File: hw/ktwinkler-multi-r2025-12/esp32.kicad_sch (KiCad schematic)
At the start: 14 parts, among them U3 ESP32-C3FH4, Y2 Q13FC13500004, Y3 XL2EL89CPI-111YLC-40M

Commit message: ktwinkler hw dev: progress stash
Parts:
- removed R3: 0R, Resistor_SMD:R_0603_1608Metric, symbol karl-atomic-basic:KR0603_0R
- added J5: Conn_01x03, Connector_PinHeader_2.54mm:PinHeader_1x03_P2.54mm_Vertical, symbol Connector_Generic:Conn_01x03
- added R3: 0R, Resistor_SMD:R_0402_1005Metric, symbol karl-atomic-basic:KR0402_0R
- added R9: 470R, Resistor_SMD:R_0402_1005Metric, symbol karl-atomic-basic:KR0402_470R
- added SW1: BOOT, Button_Switch_SMD:SW_SPST_TL3342, symbol Switch:SW_Push
- AE1: value Antenna_Dipole -> Antenna_lolpole
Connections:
- net +3V3: now also C13.1, C14.1, C2.1
- net GND: now also C13.2, C14.2, C2.2, J5.1 (Pin_1)
- net at AE1.1: now also R3.2
- net at U3.1 (LNA_IN): now also R3.1
- net at U3.27 (U0RXD): now also J5.2 (Pin_2)
- net at U3.28 (U0TXD): now also R9.2
- new net: J5.3 (Pin_3), R9.1
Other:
- note added: "double check vddspi on fh4 package"
- moved on the sheet: AE1, C13, C14, C2

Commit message: pushing onwards like a madlad
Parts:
- added C17, C7, C8: 1uF, Capacitor_SMD:C_0603_1608Metric, symbol karl-atomic-basic:KC0603_1uF
- added C18: 2.2pF, Capacitor_SMD:C_0402_1005Metric, symbol karl-atomic-basic:KC0402_2.2pF
- added J9: BWU.FL-IPEX1, Connector_Coaxial:U.FL_Hirose_U.FL-R-SMT-1_Vertical, symbol karl-parts:BWU.FL-IPEX1
- added L2: 1nH, Inductor_SMD:L_0402_1005Metric, symbol Device:L_Small
- added R10, R11, R12, R13: 10k, Resistor_SMD:R_0402_1005Metric, symbol karl-atomic-basic:KR0402_10k
- added R15, R16: 0R, Resistor_SMD:R_0402_1005Metric, symbol karl-atomic-basic:KR0402_0R
- added SW2: BOOT, Button_Switch_SMD:SW_SPST_TL3342, symbol Switch:SW_Push
- SW1: value BOOT -> RESET
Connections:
- net +3V3: now also U3.18 (VDD_SPI), C17.1, C7.1, C8.1, R10.1, R11.2, R12.1, R13.1
- net GND: now also AE1.2, SW1.2, C17.2, C18.2, C7.2, C8.2, J9.2 (Ext), L2.1, SW2.1
- net at SW1.1: now also U3.7 (CHIP_EN), R11.1
- net at U3.1 (LNA_IN): now also L2.2, R16.1; no longer R3.1
- net PWM8: now reaches U3.10 (MTDI)
- net at U3.14 (GPIO8): now also R12.2
- net at U3.15 (GPIO9): now also R13.2, SW2.2
- net PWM7: now reaches U3.16 (GPIO10)
- net PWM1: now reaches U3.19 (SPIHD)
- net PWM2: now reaches U3.20 (SPIWP)
- net PWM3: now reaches U3.21 (SPICS0)
- net PWM4: now reaches U3.22 (SPICLK)
- net PWM5: now reaches U3.23 (SPID)
- net PWM6: now reaches U3.24 (SPIQ)
- net at U3.6 (GPIO2): now also R10.2
- net MODE: now reaches U3.8 (GPIO3)
- new net: C18.1, R15.2, R16.2, R3.1
- new net: J9.1 (In), R15.1
- no-connect marks 1 -> 0
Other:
- note added: "1pair each for vdd_cpu, vdda, and vdd3p3"
- note added: "MODE is on GPIO3 as that's RTC power zone available, in case we need that for wakeups or something"
- note removed: "double check vddspi on fh4 package"
- moved on the sheet: AE1, C10, C11, C12, C13, C14, C2, C9, J5, R3, R4, R5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

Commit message: ready for scope creep
I think the schematic is ... mostly ok?  I need to decide how much of
the han p1 port scope creep to bother doing, or not...

I've roughyl blocked out the board, seems as good as any?
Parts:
- removed R11, R13: 10k, Resistor_SMD:R_0402_1005Metric, symbol karl-atomic-basic:KR0402_10k
- removed R4, R5: 0R, Resistor_SMD:R_0402_1005Metric, symbol karl-atomic-basic:KR0402_22R
- removed SW1: RESET, Button_Switch_SMD:SW_SPST_TL3342, symbol Switch:SW_Push
- removed SW2: BOOT, Button_Switch_SMD:SW_SPST_TL3342, symbol Switch:SW_Push
- removed Y3: XL2EL89CPI-111YLC-40M, Crystal:Crystal_SMD_3225-4Pin_3.2x2.5mm, symbol karl-parts:XL2EL89CPI-111YLC-40M
- added Y1: 40M, Crystal:Crystal_SMD_2016-4Pin_2.0x1.6mm, symbol karl-parts:Crystal_40M_2016_TAXM40M4ZHBCDT2T
- AE1: footprint (none) -> RF_Experiments:ANT-YOLOPOLE
- Y2: value Q13FC13500004 -> 32k
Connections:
- net GND: now also Y1.2, Y1.4
- net USBDM: now also U3.25 (GPIO18)
- net USBDP: now also U3.26 (GPIO19)
- net RESET_ESP: now reaches U3.7 (CHIP_EN)
- net GBOOT: now reaches U3.15 (GPIO9)
- net at C11.2, U3.29 (XTAL_N): now also Y1.3
- net at C12.1, U3.30 (XTAL_P): now also Y1.1

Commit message: this is just getting silly
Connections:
- net P1IN: now reaches U3.13 (MTDO)
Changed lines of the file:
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@@
+	(wire
+		(pts
+			(xy 154.94 111.76) (xy 167.64 111.76)
+		)
+		(stroke
+			(width 0)
+			(type default)
+		)
+	)
 	(wire
 		(pts
@@
 		)
 	)
+	(hierarchical_label "P1IN"
+		(shape input)
+		(at 167.64 111.76 0)
+		(effects
+			(font
+				(size 1.27 1.27)
+			)
+			(justify left)
+		)
+	)

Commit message: "schematic complete" (lol)
but yeah, i think this is most of it?  time to maybe route shit?
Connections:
- net P1_Req_Out: now reaches U3.12 (MTCK)
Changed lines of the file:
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@@
+	(wire
+		(pts
+			(xy 154.94 109.22) (xy 167.64 109.22)
+		)
+		(stroke
+			(width 0)
+			(type default)
+		)
+	)
 	(wire
 		(pts
@@
 		)
 	)
+	(hierarchical_label "P1_Req_Out"
+		(shape output)
+		(at 167.64 109.22 0)
+		(effects
+			(font
+				(size 1.27 1.27)
+			)
+			(justify left)
+		)
+	)

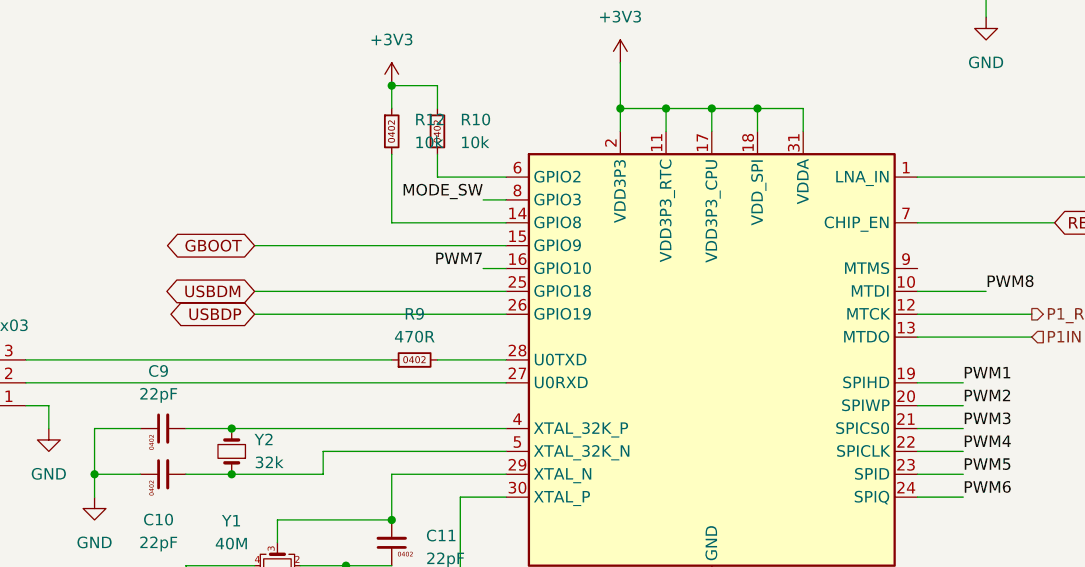
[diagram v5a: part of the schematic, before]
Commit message: update following ERC and symbol fixes
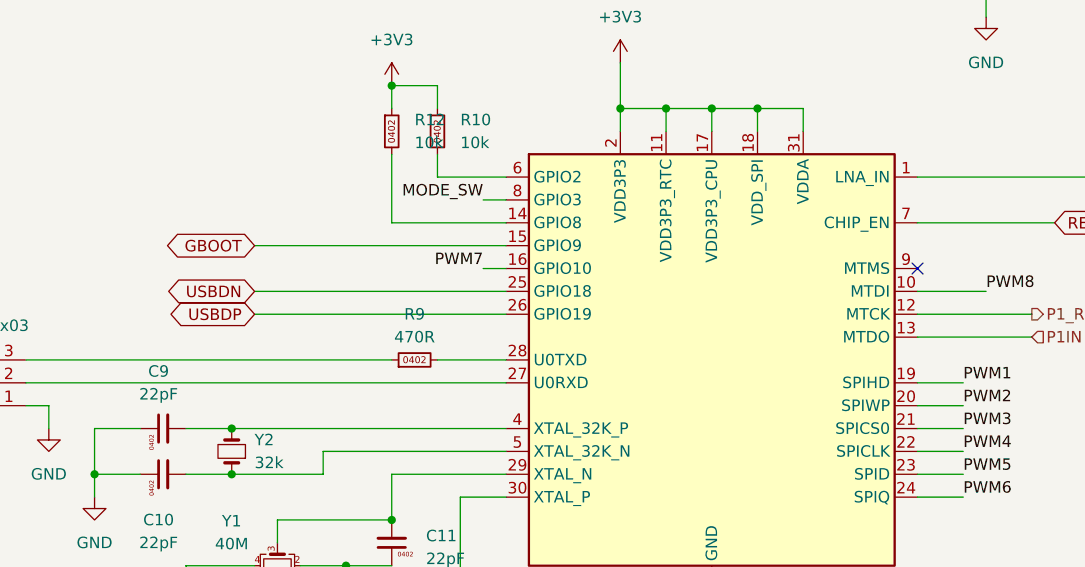
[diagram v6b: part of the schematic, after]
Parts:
- J9: symbol karl-parts:BWU.FL-IPEX1 -> karl-parts:Connector_BWU.FL-IPEX1
- Y2: symbol karl-atomic-basic:Q13FC13500004 -> karl-atomic-basic:Crystal_32k_3215_Q13FC13500004
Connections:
- net USBDM renamed USBDN
- no-connect marks 0 -> 1
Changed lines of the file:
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@@
 		(color 0 0 0 0)
 	)
+	(no_connect
+		(at 154.94 104.14)
+	)
 	(wire
 		(pts
@@
 		)
 	)
-	(global_label "USBDM"
+	(global_label "USBDN"
 		(shape bidirectional)
 		(at 81.28 106.68 180)
@@
 		)
 		(property "Intersheetrefs" "${INTERSHEET_REFS}"
-			(at 70.6521 106.68 0)
+			(at 70.773 106.68 0)
 			(effects
 				(font
@@
 	)
 	(symbol
-		(lib_id "karl-atomic-basic:Q13FC13500004")
+		(lib_id "karl-atomic-basic:Crystal_32k_3215_Q13FC13500004")
 		(at 78.74 124.46 90)
 		(unit 1)
@@
 	)
 	(symbol
-		(lib_id "karl-parts:BWU.FL-IPEX1")
+		(lib_id "karl-parts:Connector_BWU.FL-IPEX1")
 		(at 238.76 106.68 270)
 		(unit 1)

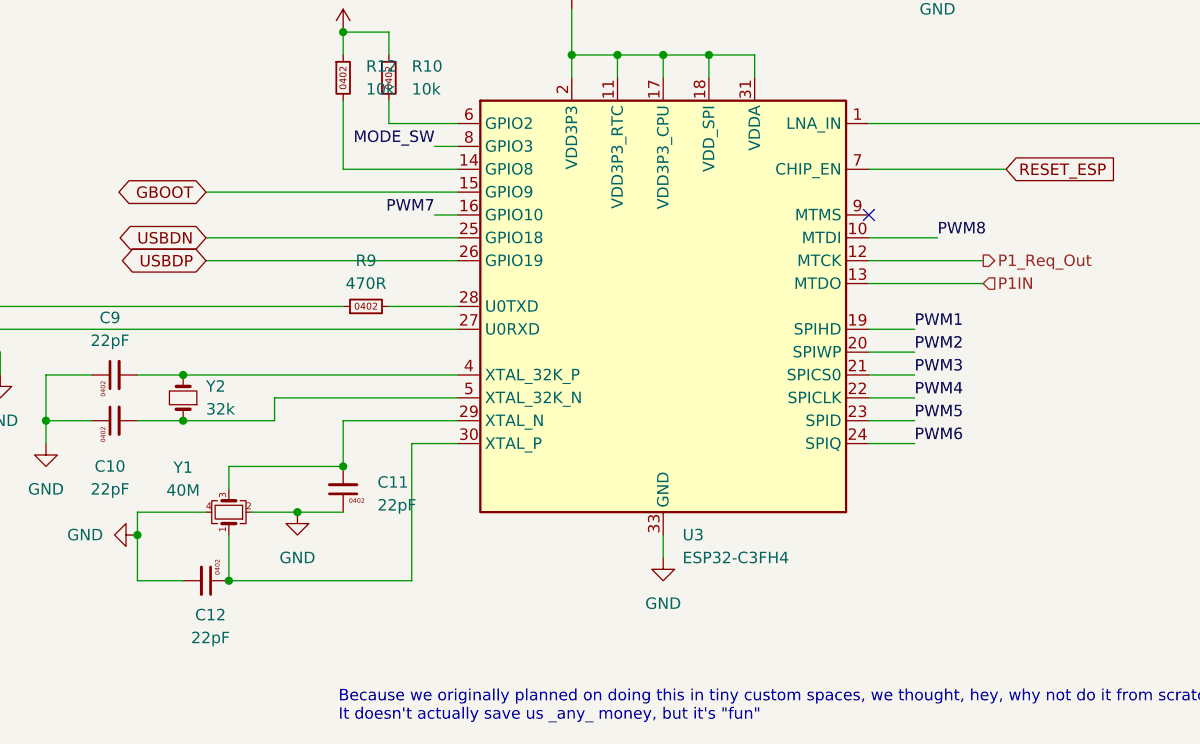
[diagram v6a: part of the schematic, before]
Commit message: streammmm updates
"complete" apart from finishing those antennas.
needs DRC cleanups on both the wch inv-f and also the yolo-pole.
need to at least _basically_ get the antenna trace basic wdith correct
as well.  yolo is fine, when it's guided yolo, not "lol"
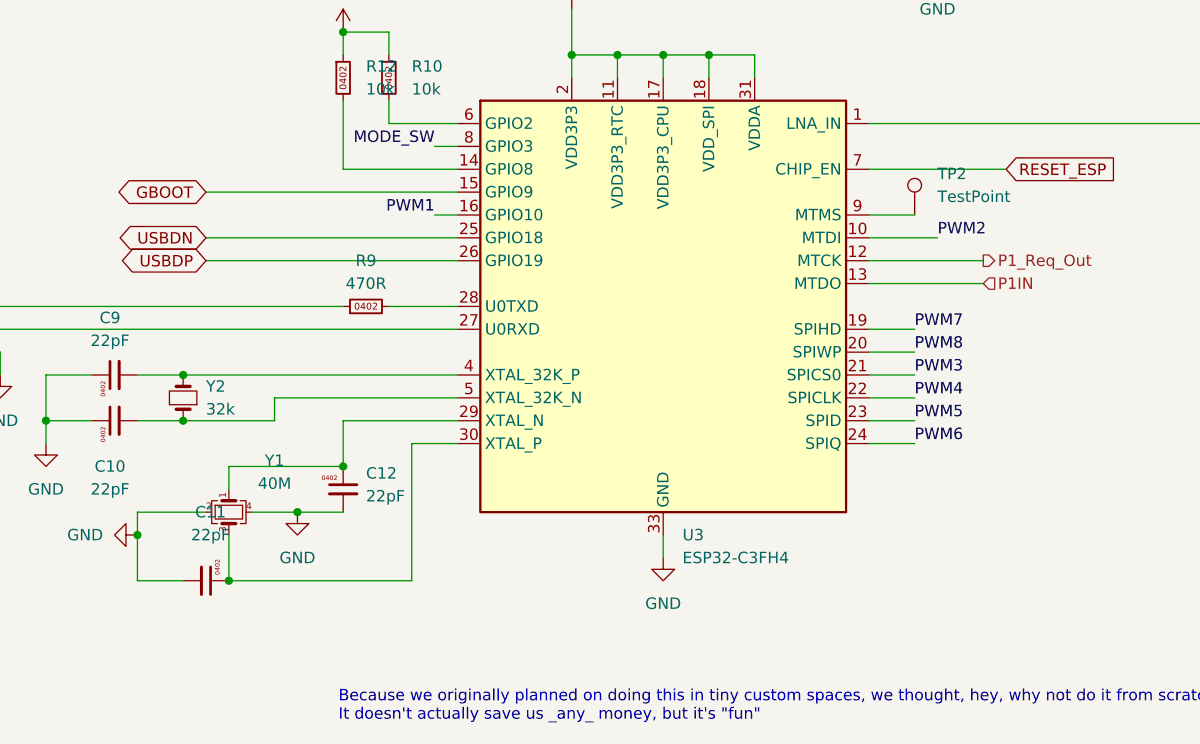
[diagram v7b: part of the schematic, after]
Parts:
- added TP2: TestPoint, TestPoint:TestPoint_THTPad_D1.0mm_Drill0.5mm, symbol Connector:TestPoint
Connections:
- net GND: now also C11.2; no longer C11.1
- net PWM1: now also U3.16 (GPIO10); no longer U3.19 (SPIHD)
- net PWM2: now also U3.10 (MTDI); no longer U3.20 (SPIWP)
- net PWM7: now also U3.19 (SPIHD); no longer U3.16 (GPIO10)
- net PWM8: now also U3.20 (SPIWP); no longer U3.10 (MTDI)
- net at C12.1, Y1.1: now also U3.29 (XTAL_N); no longer U3.30 (XTAL_P)
- net at U3.9 (MTMS): now also TP2.1
- new net: C11.1, U3.30 (XTAL_P), Y1.3
- no-connect marks 1 -> 0
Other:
- moved on the sheet: C11, C12, Y1
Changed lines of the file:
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@@
 	)
 	(junction
-		(at 96.52 132.08)
-		(diameter 0)
-		(color 0 0 0 0)
-	)
-	(junction
 		(at 238.76 93.98)
 		(diameter 0)
@@
 	)
 	(junction
+		(at 220.98 93.98)
+		(diameter 0)
+		(color 0 0 0 0)
+	)
+	(junction
 		(at 83.82 144.78)
 		(diameter 0)
@@
 	)
 	(junction
-		(at 220.98 93.98)
+		(at 96.52 132.08)
 		(diameter 0)
 		(color 0 0 0 0)
@@
 		(color 0 0 0 0)
 	)
-	(no_connect
-		(at 154.94 104.14)
-	)
 	(wire
 		(pts
@@
 	(wire
 		(pts
+			(xy 154.94 104.14) (xy 160.02 104.14)
+		)
+		(stroke
+			(width 0)
+			(type default)
+		)
+	)
+	(wire
+		(pts
 			(xy 127 86.36) (xy 132.08 86.36)
 		)
@@
 	)
 	(label "PWM1"
-		(at 160.02 116.84 0)
+		(at 106.68 104.14 180)
 		(effects
 			(font
 				(size 1.27 1.27)
 			)
-			(justify left bottom)
+			(justify right bottom)
 		)
 	)
 	(label "PWM8"
-		(at 162.56 106.68 0)
+		(at 160.02 119.38 0)
 		(effects
 			(font
@@
 	)
 	(label "PWM2"
-		(at 160.02 119.38 0)
+		(at 162.56 106.68 0)
 		(effects
 			(font
@@
 	)
 	(label "PWM7"
-		(at 106.68 104.14 180)
+		(at 160.02 116.84 0)
 		(effects
 			(font
 				(size 1.27 1.27)
 			)
-			(justify right bottom)
+			(justify left bottom)
 		)
 	)
@@
 	(symbol
 		(lib_id "karl-parts:Crystal_40M_2016_TAXM40M4ZHBCDT2T")
-		(at 83.82 137.16 90)
+		(at 83.82 137.16 270)
 		(unit 1)
 		(exclude_from_sim no)
@@
 		(fields_autoplaced yes)
 		(property "Reference" "Y1"
-			(at 78.74 132.2068 90)
+			(at 88.9 131.4382 90)
 			(effects
 				(font
@@
 		)
 		(property "Value" "40M"
-			(at 78.74 134.7468 90)
+			(at 88.9 133.9782 90)
 			(effects
 				(font
@@
 	(symbol
 		(lib_id "karl-atomic-basic:KC0402_22pF")
-		(at 96.52 134.62 180)
+		(at 81.28 144.78 270)
 		(unit 1)
 		(exclude_from_sim no)
@@
 		(fields_autoplaced yes)
 		(property "Reference" "C11"
-			(at 100.33 133.8527 0)
+			(at 81.7828 137.16 90)
 			(effects
 				(font
 					(size 1.27 1.27)
 				)
-				(justify right)
 			)
 		)
 		(property "Value" "22pF"
-			(at 100.33 136.3927 0)
+			(at 81.7828 139.7 90)
 			(effects
 				(font
 					(size 1.27 1.27)
 				)
-				(justify right)
 			)
 		)
 		(property "Footprint" "Capacitor_SMD:C_0402_1005Metric"
-			(at 97.028 130.81 0)
+			(at 77.47 144.272 0)
 			(effects
 				(font
@@
 		)
 		(property "Datasheet" "~"
-			(at 96.52 134.62 0)
+			(at 81.28 144.78 0)
 			(effects
 				(font
@@
 		)
 		(property "Description" "50V, C0G"
-			(at 96.52 130.81 0)
+			(at 77.47 144.78 0)
 			(effects
 				(font
@@
 		)
 		(property "MPN" "0402CG220J500NT"
-			(at 96.774 130.81 0)
+			(at 77.47 144.526 0)
 			(effects
 				(font
@@
 		)
 		(property "LCSC Part #" "C1555"
-			(at 96.52 130.81 0)
+			(at 77.47 144.78 0)
 			(effects
 				(font
@@
 		)
 		(property "jlcbasic" "basic"
-			(at 96.52 134.62 0)
+			(at 81.28 144.78 0)
 			(effects
 				(font
@@
 	)
 	(symbol
+		(lib_id "Connector:TestPoint")
+		(at 160.02 104.14 0)
+		(unit 1)
+		(exclude_from_sim no)
+		(in_bom yes)
+		(on_board yes)
+		(dnp no)
+		(fields_autoplaced yes)
+		(property "Reference" "TP2"
+			(at 162.56 99.5679 0)
+			(effects
+				(font
+					(size 1.27 1.27)
+				)
+				(justify left)
+			)
+		)
+		(property "Value" "TestPoint"
+			(at 162.56 102.1079 0)
+			(effects
+				(font
+					(size 1.27 1.27)
+				)
+				(justify left)
+			)
+		)
+		(property "Footprint" "TestPoint:TestPoint_THTPad_D1.0mm_Drill0.5mm"
+			(at 165.1 104.14 0)
+			(effects
+				(font
+					(size 1.27 1.27)
+				)
+				(hide yes)
+			)
+		)
+		(property "Datasheet" "~"
+			(at 165.1 104.14 0)
+			(effects
+				(font
+					(size 1.27 1.27)
+				)
+				(hide yes)
+			)
+		)
+		(property "Description" "test point"
+			(at 160.02 104.14 0)
+			(effects
+				(font
+					(size 1.27 1.27)
+				)
+				(hide yes)
+			)
+		)
+		(pin "1"
+		)
+		(instances
+			(project "ktwinkler-multi-r2025-12"
+				(path "/48773b41-b773-40e2-8ba4-2e78c7a3e45f/f1fab45e-2489-4bf6-8b0f-5e1748a9ff79"
+					(reference "TP2")
+					(unit 1)
+				)
+			)
+		)
+	)
+	(symbol
 		(lib_id "karl-atomic-basic:KC0402_100nF_16V")
 		(at 172.72 68.58 0)
@@
 	(symbol
 		(lib_id "karl-atomic-basic:KC0402_22pF")
-		(at 81.28 144.78 270)
+		(at 96.52 134.62 0)
 		(unit 1)
 		(exclude_from_sim no)
@@
 		(fields_autoplaced yes)
 		(property "Reference" "C12"
-			(at 81.7828 148.59 90)
+			(at 99.06 132.8471 0)
 			(effects
 				(font
 					(size 1.27 1.27)
 				)
+				(justify left)
 			)
 		)
 		(property "Value" "22pF"
-			(at 81.7828 151.13 90)
+			(at 99.06 135.3871 0)
 			(effects
 				(font
 					(size 1.27 1.27)
 				)
+				(justify left)
 			)
 		)
 		(property "Footprint" "Capacitor_SMD:C_0402_1005Metric"
-			(at 77.47 144.272 0)
+			(at 96.012 138.43 0)
 			(effects
 				(font
@@
 		)
 		(property "Datasheet" "~"
-			(at 81.28 144.78 0)
+			(at 96.52 134.62 0)
 			(effects
 				(font
@@
 		)
 		(property "Description" "50V, C0G"
-			(at 77.47 144.78 0)
+			(at 96.52 138.43 0)
 			(effects
 				(font
@@
 		)
 		(property "MPN" "0402CG220J500NT"
-			(at 77.47 144.526 0)
+			(at 96.266 138.43 0)
 			(effects
 				(font
@@
 		)
 		(property "LCSC Part #" "C1555"
-			(at 77.47 144.78 0)
+			(at 96.52 138.43 0)
 			(effects
 				(font
@@
 		)
 		(property "jlcbasic" "basic"
-			(at 81.28 144.78 0)
+			(at 96.52 134.62 0)
 			(effects
 				(font

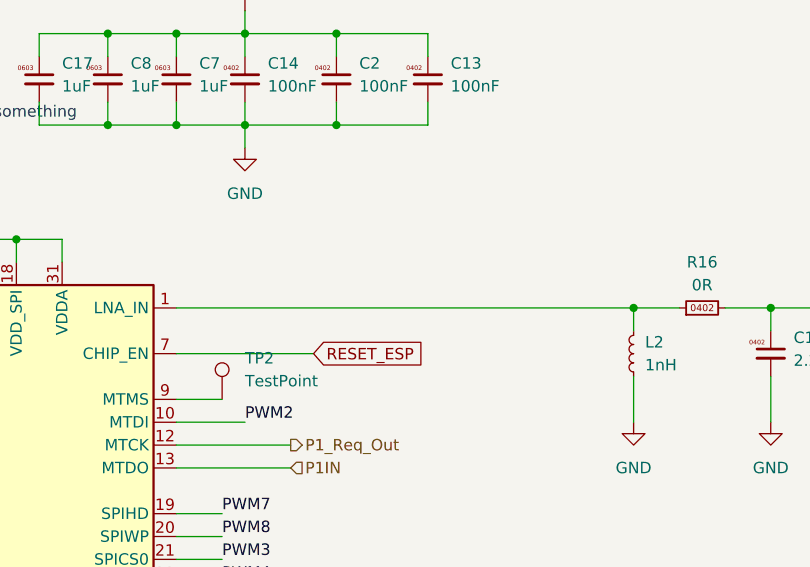
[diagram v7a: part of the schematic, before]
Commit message: hw: update to kicad 10 and order
We added a late qwiic connector to the ch584 side, why not, try that out
too.  We also fixed our smtso footprint, we hope...

Fuck poking the rf more, we're yolo-poling...
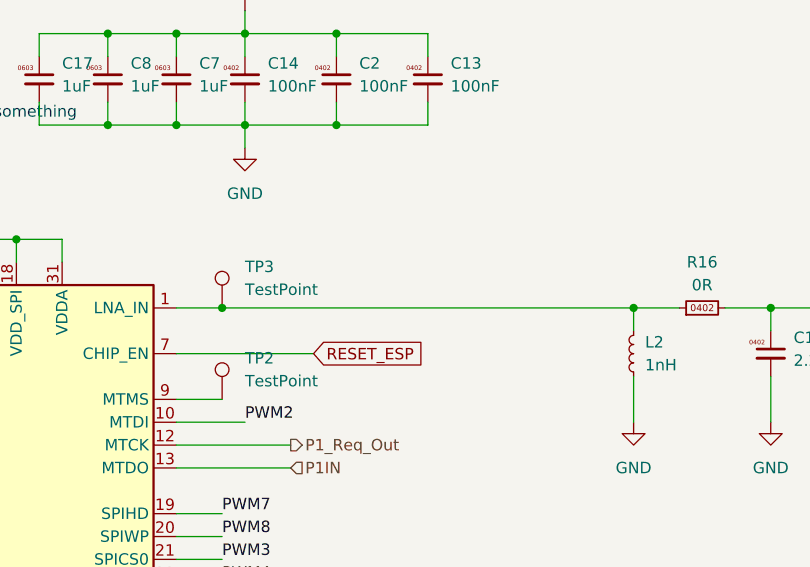
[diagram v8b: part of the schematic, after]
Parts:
- added TP3: TestPoint, TestPoint:TestPoint_Pad_D1.0mm, symbol Connector:TestPoint
- AE1, TP2: now left out of the parts list
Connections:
- net at L2.2, R16.1, U3.1 (LNA_IN): now also TP3.1
